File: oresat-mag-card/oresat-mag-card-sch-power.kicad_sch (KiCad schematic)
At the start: 88 parts, among them Q1 DMP2240UDM, Q2 PMV45EN, Q3 DMP3050LVT-7, Q4 DMP3050LVT-7, Q5 PMV45EN, U1 MAX7310, U2 MIC842LYC5, U3 MIC842LYC5, U4 TS5A21366DCUR, U5 MAX4211FETE, U6 TPS62111RSA

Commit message: Small update
removed all traces containing widths of .127 and widened to .2, and some other small misc items
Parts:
- R1, R10, R11, R12, R13, R14, R15, R16, R17, R19, R2, R20, R21, R22, R25, R27, R28, R29, R3, R33, R35, R36, R37, R38, R4, R5, R6, R7, R8, R9: footprint Resistor_SMD:R_0603_1608Metric -> oresat-passives:c_0603-SMALL
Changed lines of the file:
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@@
 			)
 		)
-		(property "Footprint" "Resistor_SMD:R_0603_1608Metric"
+		(property "Footprint" "oresat-passives:c_0603-SMALL"
 			(at 138.43 160.02 0)
 			(effects
@@
 			)
 		)
-		(property "Footprint" "Resistor_SMD:R_0603_1608Metric"
+		(property "Footprint" "oresat-passives:c_0603-SMALL"
 			(at 156.21 306.07 0)
 			(effects
@@
 			)
 		)
-		(property "Footprint" "Resistor_SMD:R_0603_1608Metric"
+		(property "Footprint" "oresat-passives:c_0603-SMALL"
 			(at 128.27 171.45 0)
 			(effects
@@
 			)
 		)
-		(property "Footprint" "Resistor_SMD:R_0603_1608Metric"
+		(property "Footprint" "oresat-passives:c_0603-SMALL"
 			(at 163.83 306.07 0)
 			(effects
@@
 			)
 		)
-		(property "Footprint" "Resistor_SMD:R_0603_1608Metric"
+		(property "Footprint" "oresat-passives:c_0603-SMALL"
 			(at 123.19 170.18 0)
 			(effects
@@
 			)
 		)
-		(property "Footprint" "Resistor_SMD:R_0603_1608Metric"
+		(property "Footprint" "oresat-passives:c_0603-SMALL"
 			(at 106.68 127 0)
 			(effects
@@
 			)
 		)
-		(property "Footprint" "Resistor_SMD:R_0603_1608Metric"
+		(property "Footprint" "oresat-passives:c_0603-SMALL"
 			(at 143.51 170.18 0)
 			(effects
@@
 			)
 		)
-		(property "Footprint" "Resistor_SMD:R_0603_1608Metric"
+		(property "Footprint" "oresat-passives:c_0603-SMALL"
 			(at 306.07 151.13 0)
 			(effects
@@
 			)
 		)
-		(property "Footprint" "Resistor_SMD:R_0603_1608Metric"
+		(property "Footprint" "oresat-passives:c_0603-SMALL"
 			(at 379.73 132.08 0)
 			(effects
@@
 			)
 		)
-		(property "Footprint" "Resistor_SMD:R_0603_1608Metric"
+		(property "Footprint" "oresat-passives:c_0603-SMALL"
 			(at 392.43 137.16 0)
 			(effects
@@
 			)
 		)
-		(property "Footprint" "Resistor_SMD:R_0603_1608Metric"
+		(property "Footprint" "oresat-passives:c_0603-SMALL"
 			(at 107.95 160.02 0)
 			(effects
@@
 			)
 		)
-		(property "Footprint" "Resistor_SMD:R_0603_1608Metric"
+		(property "Footprint" "oresat-passives:c_0603-SMALL"
 			(at 248.92 165.1 0)
 			(effects
@@
 			)
 		)
-		(property "Footprint" "Resistor_SMD:R_0603_1608Metric"
+		(property "Footprint" "oresat-passives:c_0603-SMALL"
 			(at 128.27 160.02 0)
 			(effects
@@
 			)
 		)
-		(property "Footprint" "Resistor_SMD:R_0603_1608Metric"
+		(property "Footprint" "oresat-passives:c_0603-SMALL"
 			(at 351.79 327.66 0)
 			(effects
@@
 			)
 		)
-		(property "Footprint" "Resistor_SMD:R_0603_1608Metric"
+		(property "Footprint" "oresat-passives:c_0603-SMALL"
 			(at 113.03 160.02 0)
 			(effects
@@
 			)
 		)
-		(property "Footprint" "Resistor_SMD:R_0603_1608Metric"
+		(property "Footprint" "oresat-passives:c_0603-SMALL"
 			(at 156.21 350.52 0)
 			(effects
@@
 			)
 		)
-		(property "Footprint" "Resistor_SMD:R_0603_1608Metric"
+		(property "Footprint" "oresat-passives:c_0603-SMALL"
 			(at 143.51 160.02 0)
 			(effects
@@
 			)
 		)
-		(property "Footprint" "Resistor_SMD:R_0603_1608Metric"
+		(property "Footprint" "oresat-passives:c_0603-SMALL"
 			(at 140.97 330.2 0)
 			(effects
@@
 			)
 		)
-		(property "Footprint" "Resistor_SMD:R_0603_1608Metric"
+		(property "Footprint" "oresat-passives:c_0603-SMALL"
 			(at 163.83 350.52 0)
 			(effects
@@
 			)
 		)
-		(property "Footprint" "Resistor_SMD:R_0603_1608Metric"
+		(property "Footprint" "oresat-passives:c_0603-SMALL"
 			(at 138.43 170.18 0)
 			(effects
@@
 			)
 		)
-		(property "Footprint" "Resistor_SMD:R_0603_1608Metric"
+		(property "Footprint" "oresat-passives:c_0603-SMALL"
 			(at 140.97 374.65 0)
 			(effects
@@
 			)
 		)
-		(property "Footprint" "Resistor_SMD:R_0603_1608Metric"
+		(property "Footprint" "oresat-passives:c_0603-SMALL"
 			(at 114.3 354.33 0)
 			(effects
@@
 			)
 		)
-		(property "Footprint" "Resistor_SMD:R_0603_1608Metric"
+		(property "Footprint" "oresat-passives:c_0603-SMALL"
 			(at 114.3 309.88 0)
 			(effects
@@
 			)
 		)
-		(property "Footprint" "Resistor_SMD:R_0603_1608Metric"
+		(property "Footprint" "oresat-passives:c_0603-SMALL"
 			(at 113.03 170.18 0)
 			(effects
@@
 			)
 		)
-		(property "Footprint" "Resistor_SMD:R_0603_1608Metric"
+		(property "Footprint" "oresat-passives:c_0603-SMALL"
 			(at 107.95 170.18 0)
 			(effects
@@
 			)
 		)
-		(property "Footprint" "Resistor_SMD:R_0603_1608Metric"
+		(property "Footprint" "oresat-passives:c_0603-SMALL"
 			(at 373.38 139.7 0)
 			(effects
@@
 			)
 		)
-		(property "Footprint" "Resistor_SMD:R_0603_1608Metric"
+		(property "Footprint" "oresat-passives:c_0603-SMALL"
 			(at 379.73 154.94 0)
 			(effects
@@
 			)
 		)
-		(property "Footprint" "Resistor_SMD:R_0603_1608Metric"
+		(property "Footprint" "oresat-passives:c_0603-SMALL"
 			(at 290.83 228.6 0)
 			(effects
@@
 			)
 		)
-		(property "Footprint" "Resistor_SMD:R_0603_1608Metric"
+		(property "Footprint" "oresat-passives:c_0603-SMALL"
 			(at 290.83 233.68 0)
 			(effects
@@
 			)
 		)
-		(property "Footprint" "Resistor_SMD:R_0603_1608Metric"
+		(property "Footprint" "oresat-passives:c_0603-SMALL"
 			(at 123.19 160.02 0)
 			(effects

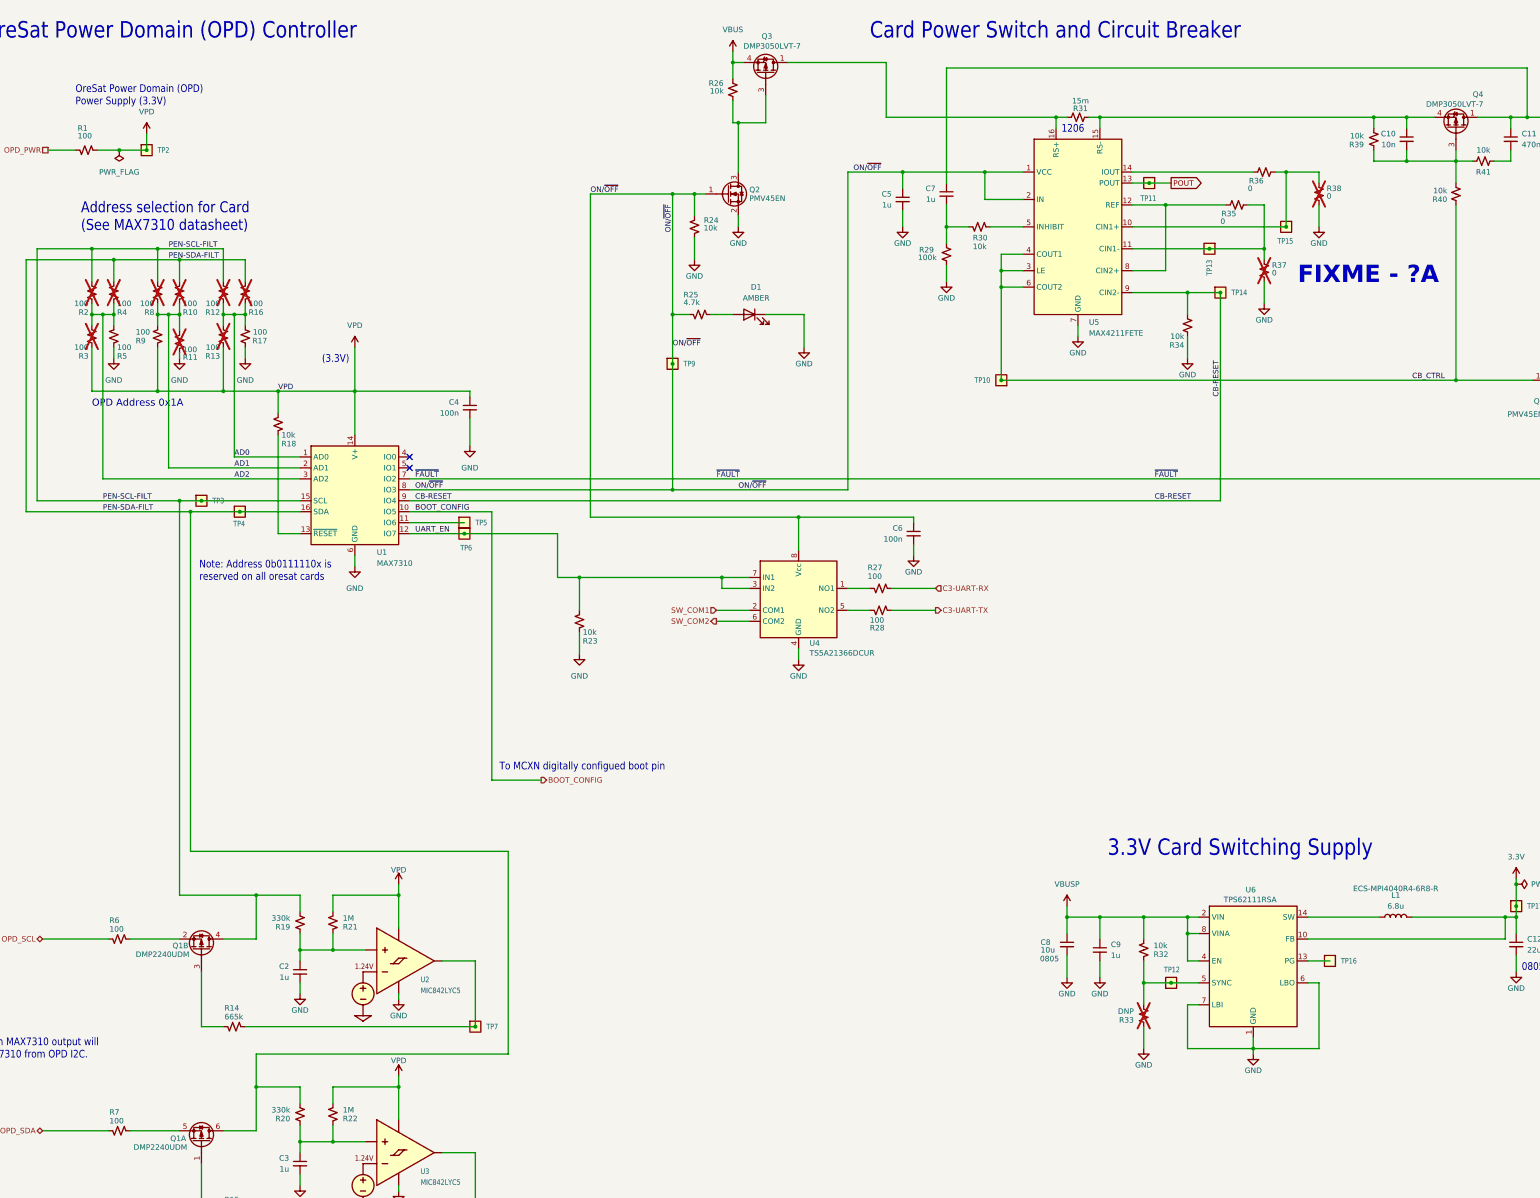
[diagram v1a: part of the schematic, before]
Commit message: Update
Updated footprints, symbols, and pcb layout to have IMU in center of board.
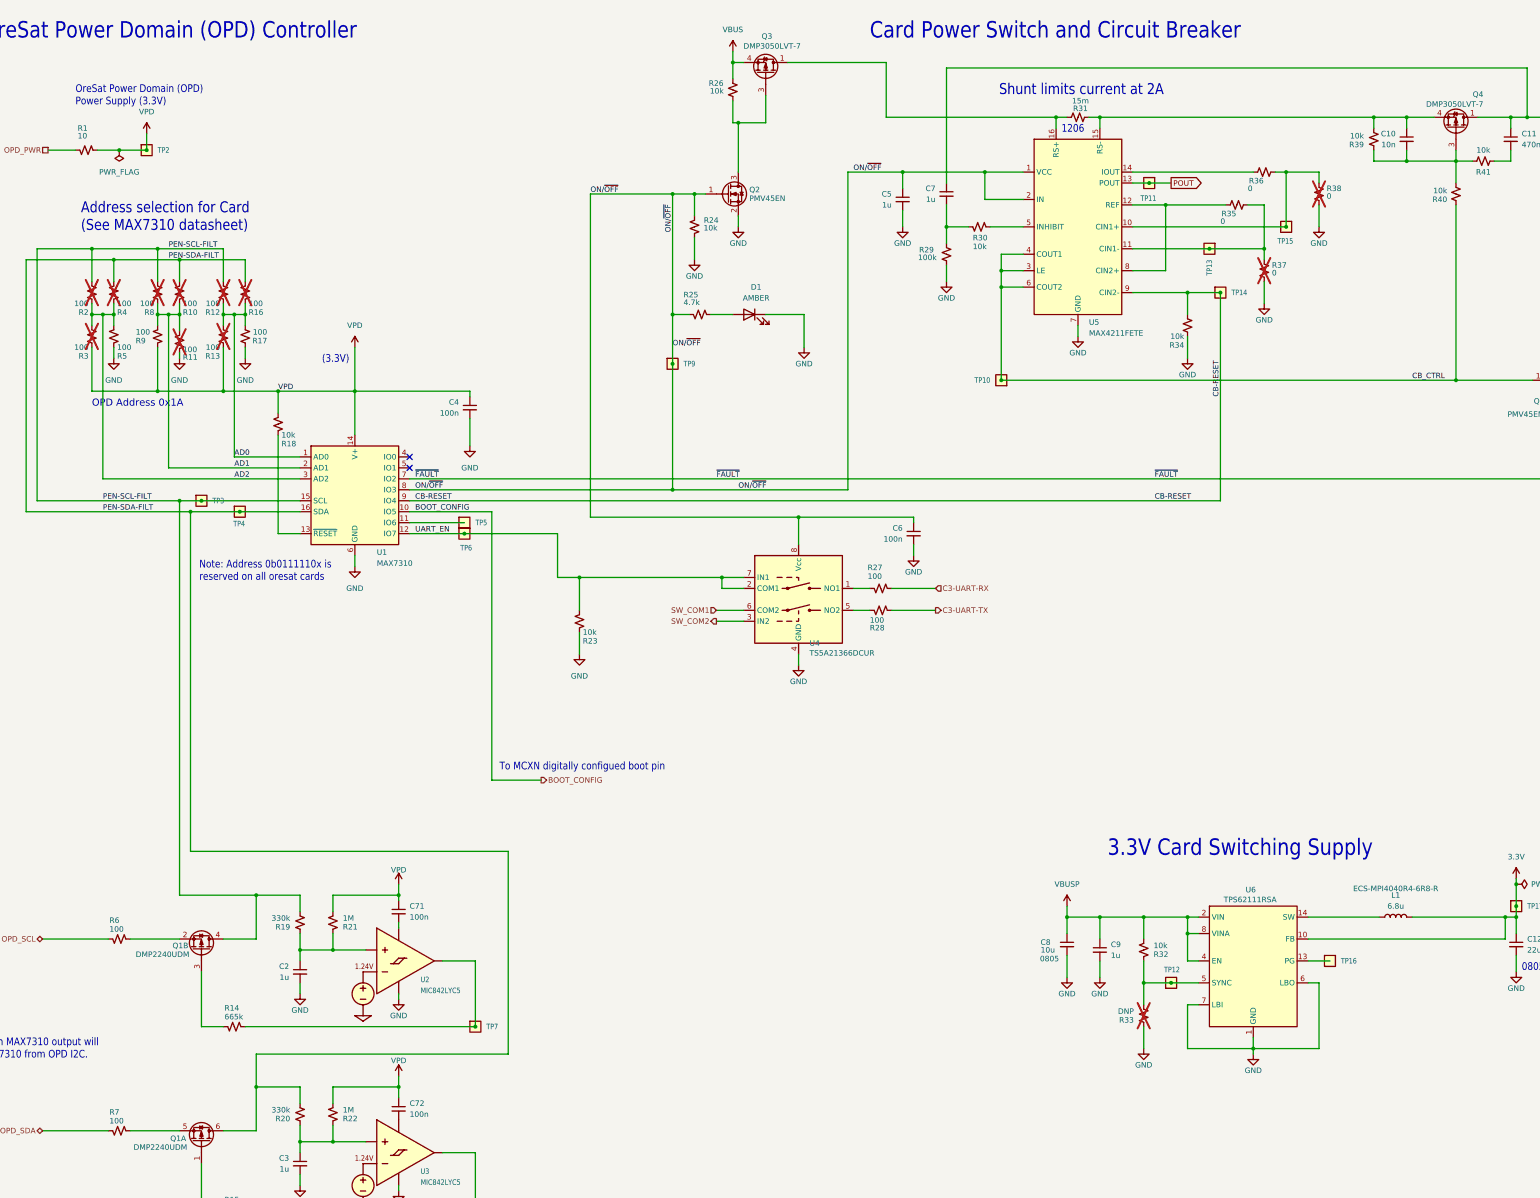
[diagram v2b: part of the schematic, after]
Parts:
- added C71, C72: 100n, oresat-passives:c_0603-SMALL, symbol Device:C_Small
- R1: value 100 -> 10
- U4: DIS (none) -> DigiKey; DPN (none) -> 296-24304-1-ND; MFR (none) -> Texas Instruments; MPN (none) -> TS5A21366DCUR
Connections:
- net SW_COM1: now also U4.6 (COM2); no longer U4.2 (COM1)
- net SW_COM2: now also U4.3 (IN2); no longer U4.6 (COM2)
- net UART_EN: now also U4.2 (COM1); no longer U4.3 (IN2)
- net VPD: now also C71.1, C72.1; no longer U2.5 (VDD), U3.5 (VDD)
- new net: C71.2, U2.5 (VDD)
- new net: C72.2, U3.5 (VDD)
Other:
- note added: "Shunt limits current at 2A"
- note removed: "FIXME - ?A"

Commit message: Final touch ups
Added new j3 connector, and final touch ups
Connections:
- net GND: now also C71.2, C72.2
- net VPD: now also U2.5 (VDD), U3.5 (VDD)
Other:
- moved on the sheet: C71, C72
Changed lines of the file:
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@@
 	)
 	(junction
-		(at 179.07 299.72)
-		(diameter 0)
-		(color 0 0 0 0)
-	)
-	(junction
 		(at 163.83 356.87)
 		(diameter 0)
@@
 	)
 	(junction
-		(at 384.81 132.08)
+		(at 179.07 299.72)
 		(diameter 0)
 		(color 0 0 0 0)
 	)
 	(junction
-		(at 123.19 165.1)
+		(at 384.81 132.08)
 		(diameter 0)
 		(color 0 0 0 0)
 	)
 	(junction
-		(at 179.07 344.17)
+		(at 123.19 165.1)
 		(diameter 0)
 		(color 0 0 0 0)
@@
 	)
 	(junction
+		(at 179.07 344.17)
+		(diameter 0)
+		(color 0 0 0 0)
+	)
+	(junction
 		(at 471.17 115.57)
 		(diameter 0)
@@
 	(wire
 		(pts
-			(xy 179.07 344.17) (xy 179.07 346.71)
-		)
-		(stroke
-			(width 0)
-			(type default)
-		)
-	)
-	(wire
-		(pts
 			(xy 156.21 344.17) (xy 156.21 347.98)
 		)
@@
 	(wire
 		(pts
+			(xy 186.69 299.72) (xy 179.07 299.72)
+		)
+		(stroke
+			(width 0)
+			(type default)
+		)
+	)
+	(wire
+		(pts
 			(xy 436.88 119.38) (xy 436.88 121.92)
 		)
@@
 	(wire
 		(pts
+			(xy 179.07 351.79) (xy 179.07 344.17)
+		)
+		(stroke
+			(width 0)
+			(type default)
+		)
+	)
+	(wire
+		(pts
 			(xy 107.95 162.56) (xy 107.95 165.1)
 		)
@@
 	(wire
 		(pts
+			(xy 179.07 307.34) (xy 179.07 299.72)
+		)
+		(stroke
+			(width 0)
+			(type default)
+		)
+	)
+	(wire
+		(pts
 			(xy 242.57 137.16) (xy 223.52 137.16)
 		)
@@
 	(wire
 		(pts
+			(xy 186.69 300.99) (xy 186.69 299.72)
+		)
+		(stroke
+			(width 0)
+			(type default)
+		)
+	)
+	(wire
+		(pts
 			(xy 151.13 182.88) (xy 168.91 182.88)
 		)
@@
 	(wire
 		(pts
+			(xy 186.69 306.07) (xy 186.69 308.61)
+		)
+		(stroke
+			(width 0)
+			(type default)
+		)
+	)
+	(wire
+		(pts
 			(xy 295.91 132.08) (xy 314.96 132.08)
 		)
@@
 	(wire
 		(pts
+			(xy 191.77 354.33) (xy 191.77 351.79)
+		)
+		(stroke
+			(width 0)
+			(type default)
+		)
+	)
+	(wire
+		(pts
 			(xy 292.1 119.38) (xy 292.1 106.68)
 		)
@@
 	(wire
 		(pts
+			(xy 191.77 344.17) (xy 191.77 346.71)
+		)
+		(stroke
+			(width 0)
+			(type default)
+		)
+	)
+	(wire
+		(pts
 			(xy 414.02 304.8) (xy 435.61 304.8)
 		)
@@
 	(wire
 		(pts
-			(xy 179.07 307.34) (xy 179.07 306.07)
-		)
-		(stroke
-			(width 0)
-			(type default)
-		)
-	)
-	(wire
-		(pts
 			(xy 120.65 127) (xy 120.65 123.19)
 		)
@@
 	(wire
 		(pts
-			(xy 179.07 300.99) (xy 179.07 299.72)
+			(xy 143.51 165.1) (xy 140.97 165.1)
 		)
 		(stroke
@@
 	(wire
 		(pts
-			(xy 143.51 165.1) (xy 140.97 165.1)
+			(xy 191.77 344.17) (xy 179.07 344.17)
 		)
 		(stroke
@@
 	)
 	(symbol
+		(lib_name "GND_1")
+		(lib_id "power:GND")
+		(at 186.69 308.61 0)
+		(unit 1)
+		(exclude_from_sim no)
+		(in_bom yes)
+		(on_board yes)
+		(dnp no)
+		(property "Reference" "#GND0105"
+			(at 186.69 314.96 0)
+			(effects
+				(font
+					(size 1.27 1.27)
+				)
+				(hide yes)
+			)
+		)
+		(property "Value" "GND"
+			(at 186.69 312.42 0)
+			(effects
+				(font
+					(size 1.27 1.27)
+				)
+			)
+		)
+		(property "Footprint" ""
+			(at 186.69 308.61 0)
+			(effects
+				(font
+					(size 1.27 1.27)
+				)
+				(hide yes)
+			)
+		)
+		(property "Datasheet" ""
+			(at 186.69 308.61 0)
+			(effects
+				(font
+					(size 1.27 1.27)
+				)
+				(hide yes)
+			)
+		)
+		(property "Description" "Power symbol creates a global label with name \"GND\" , ground"
+			(at 186.69 308.61 0)
+			(effects
+				(font
+					(size 1.27 1.27)
+				)
+				(hide yes)
+			)
+		)
+		(pin "1"
+		)
+		(instances
+			(project "oresat-mag-card"
+				(path "/c58960d9-4cac-4036-ad2e-1aef26946dae/2e7c06c0-a412-4c3a-b490-9aec08573322"
+					(reference "#GND0105")
+					(unit 1)
+				)
+			)
+		)
+	)
+	(symbol
 		(lib_id "oresat-misc:Test-Point-0.75mm-th")
 		(at 120.65 127 0)
@@
 	)
 	(symbol
+		(lib_name "GND_1")
+		(lib_id "power:GND")
+		(at 191.77 354.33 0)
+		(unit 1)
+		(exclude_from_sim no)
+		(in_bom yes)
+		(on_board yes)
+		(dnp no)
+		(property "Reference" "#GND0106"
+			(at 191.77 360.68 0)
+			(effects
+				(font
+					(size 1.27 1.27)
+				)
+				(hide yes)
+			)
+		)
+		(property "Value" "GND"
+			(at 191.77 358.14 0)
+			(effects
+				(font
+					(size 1.27 1.27)
+				)
+			)
+		)
+		(property "Footprint" ""
+			(at 191.77 354.33 0)
+			(effects
+				(font
+					(size 1.27 1.27)
+				)
+				(hide yes)
+			)
+		)
+		(property "Datasheet" ""
+			(at 191.77 354.33 0)
+			(effects
+				(font
+					(size 1.27 1.27)
+				)
+				(hide yes)
+			)
+		)
+		(property "Description" "Power symbol creates a global label with name \"GND\" , ground"
+			(at 191.77 354.33 0)
+			(effects
+				(font
+					(size 1.27 1.27)
+				)
+				(hide yes)
+			)
+		)
+		(pin "1"
+		)
+		(instances
+			(project "oresat-mag-card"
+				(path "/c58960d9-4cac-4036-ad2e-1aef26946dae/2e7c06c0-a412-4c3a-b490-9aec08573322"
+					(reference "#GND0106")
+					(unit 1)
+				)
+			)
+		)
+	)
+	(symbol
 		(lib_id "oresat-misc:Test-Point-0.75mm-th")
 		(at 394.97 314.96 90)
@@
 		(dnp no)
 		(property "Reference" "U4"
-			(at 274.32 241.3 0)
+			(at 274.828 243.332 0)
 			(effects
 				(font
@@
 		)
 		(property "Value" "TS5A21366DCUR"
-			(at 274.32 243.586 0)
+			(at 274.828 245.618 0)
 			(effects
 				(font
@@
 	(symbol
 		(lib_id "Device:C_Small")
-		(at 179.07 303.53 0)
+		(at 186.69 303.53 0)
 		(unit 1)
 		(exclude_from_sim no)
@@
 		(dnp no)
 		(property "Reference" "C71"
-			(at 181.61 302.2662 0)
+			(at 189.23 302.2662 0)
 			(effects
 				(font
@@
 		)
 		(property "Value" "100n"
-			(at 181.61 304.8062 0)
+			(at 189.23 304.8062 0)
 			(effects
 				(font
@@
 		)
 		(property "Footprint" "oresat-passives:c_0603-SMALL"
-			(at 179.07 303.53 0)
+			(at 186.69 303.53 0)
 			(effects
 				(font
@@
 		)
 		(property "Datasheet" "~"
-			(at 179.07 303.53 0)
+			(at 186.69 303.53 0)
 			(effects
 				(font
@@
 		)
 		(property "Description" ""
-			(at 179.07 303.53 0)
+			(at 186.69 303.53 0)
 			(effects
 				(font
@@
 		)
 		(property "DIST" ""
-			(at 179.07 303.53 0)
+			(at 186.69 303.53 0)
 			(effects
 				(font
@@
 					(size 1.27 1.27)
 				)
+				(hide yes)
 			)
 		)
@@
 	(symbol
 		(lib_id "Device:C_Small")
-		(at 179.07 349.25 0)
+		(at 191.77 349.25 0)
 		(unit 1)
 		(exclude_from_sim no)
@@
 		(dnp no)
 		(property "Reference" "C72"
-			(at 181.61 347.9862 0)
+			(at 194.31 347.9862 0)
 			(effects
 				(font
@@
 		)
 		(property "Value" "100n"
-			(at 181.61 350.5262 0)
+			(at 194.31 350.5262 0)
 			(effects
 				(font
@@
 		)
 		(property "Footprint" "oresat-passives:c_0603-SMALL"
-			(at 179.07 349.25 0)
+			(at 191.77 349.25 0)
 			(effects
 				(font
@@
 		)
 		(property "Datasheet" "~"
-			(at 179.07 349.25 0)
+			(at 191.77 349.25 0)
 			(effects
 				(font
@@
 		)
 		(property "Description" ""
-			(at 179.07 349.25 0)
+			(at 191.77 349.25 0)
 			(effects
 				(font
@@
 		)
 		(property "DIST" ""
-			(at 179.07 349.25 0)
+			(at 191.77 349.25 0)
 			(effects
 				(font

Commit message: Schematic polish, fixed UART TX/RX mixup, imported into layout
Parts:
- removed TP6: Test-Point, oresat-misc:TestPoint-0.75mm-th, symbol oresat-misc:Test-Point-0.75mm-th
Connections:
- net SW_COM2 is gone; now on net UART_EN: U4.3 (IN2)
- net UART_EN: no longer U4.2 (COM1)
- net SW_COM1 renamed CARD-UART-RX
- new net CARD-UART-TX: U4.2 (COM1)
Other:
- note added: "All caps are 0603 ceramic 10% X5R >= 16V Vwv and AEQ unless marked"
- note added: "All resistors 0603 +/- 1% and AEQ unless marked"
- note added: "Shunt limits current to 2A"
- note removed: "Note: Address 0b0111110x is reserved on all oresat cards"
- note removed: "Shunt limits current at 2A"
- note removed: "To MCXN digitally configued boot pin"
- company: Edward Tsoi -> Portland State Aerospace Society
- title: OreSat ADCS Card -> OreSat Mag Card
- moved on the sheet: C12, C6, D2, L1, R23, R27, R28, R43, TP17, U4

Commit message: No DRC errors
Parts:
- C10, C11, C2, C3, C4, C5, C6, C7, C71, C72, C9, R1, R10, R11, R12, R13, R14, R15, R16, R17, R19, R2, R20, R21, R22, R25, R27, R28, R29, R3, R33, R35, R36, R37, R38, R4, R5, R6, R7, R8, R9: footprint oresat-passives:c_0603-SMALL -> oresat-passives:0603-C-NOSILK
- L1: footprint oresat-acs-card:ECS-MPI4040 -> oresat-passives:L_ECS-MPI4040
- R18, R23, R24, R26, R30, R32, R34, R39, R40, R41, R42, R43, R44: footprint Resistor_SMD:R_0603_1608Metric -> oresat-passives:0603-C-NOSILK
- R31: footprint oresat-acs-card:R1206 -> oresat-passives:1206-C
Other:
- moved on the sheet: C10, C11, C12, C2, C3, C4, C5, C6, C7, C71, C72, C8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
